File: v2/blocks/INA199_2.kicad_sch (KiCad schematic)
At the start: 3 parts, among them U16 20m 1206, U17 INA199A1DCKR

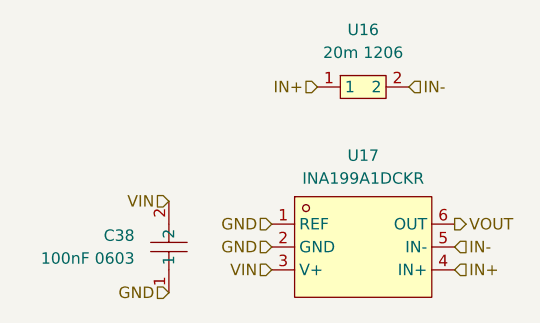
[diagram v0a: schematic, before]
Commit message: preliminary layout
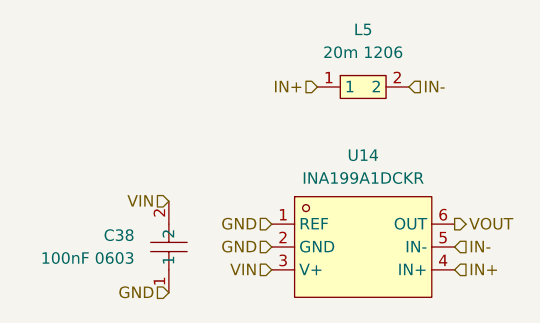
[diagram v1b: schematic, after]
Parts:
- renumbered U16 to L5, U17 to U14
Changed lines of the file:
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@@
 		(dnp no)
 		(fields_autoplaced yes)
-		(property "Reference" "U16"
+		(property "Reference" "L5"
 			(at 119.38 66.04 0)
 			(effects
@@
 			(project "EPSv2"
 				(path "/61d36b12-c329-4dd2-b08b-b63678fc7b25/318efe62-29b8-42d0-b5fb-0df2aae93ba9"
-					(reference "U16")
+					(reference "L5")
 					(unit 1)
 				)
@@
 		(dnp no)
 		(fields_autoplaced yes)
-		(property "Reference" "U17"
+		(property "Reference" "U14"
 			(at 119.38 80.01 0)
 			(effects
@@
 			(project "EPSv2"
 				(path "/61d36b12-c329-4dd2-b08b-b63678fc7b25/318efe62-29b8-42d0-b5fb-0df2aae93ba9"
-					(reference "U17")
+					(reference "U14")
 					(unit 1)
 				)

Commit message: battery charging routing
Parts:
- renumbered C38 to C30
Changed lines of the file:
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@@
 		(dnp no)
 		(fields_autoplaced yes)
-		(property "Reference" "C38"
+		(property "Reference" "C30"
 			(at 93.98 88.9 90)
 			(effects
@@
 			(project "EPSv2"
 				(path "/61d36b12-c329-4dd2-b08b-b63678fc7b25/318efe62-29b8-42d0-b5fb-0df2aae93ba9"
-					(reference "C38")
+					(reference "C30")
 					(unit 1)
 				)
